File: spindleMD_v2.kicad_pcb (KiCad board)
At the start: 2 copper layers, 72 x 95 mm, 99 parts, among them J1 Conn_LogicPower, J2 Conn_SWD, J3 Conn_UART, J4 Conn_I2C, J5 Conn_Encoder, J6 Conn_GPIO, J7 Conn_MotorPower, J8 Conn_drivePower, J9 Conn_Motor, Q1 Q_NMOS_GDS, Q2 Q_NMOS_GDS, Q3 Q_NMOS_GDS, Q4 Q_NMOS_GDS, SW1 USER_BUTTON, SW2 RESET_BUTTON, U1 L7805, U10 ADuM3190, U2 L78L33_SOT89, U3 IK0505SA, U4 STM32F303K8Tx, U5 TLP152, U6 TLP152, U7 TLP152, U8 TLP152, U9 ACS712xLCTR-30A

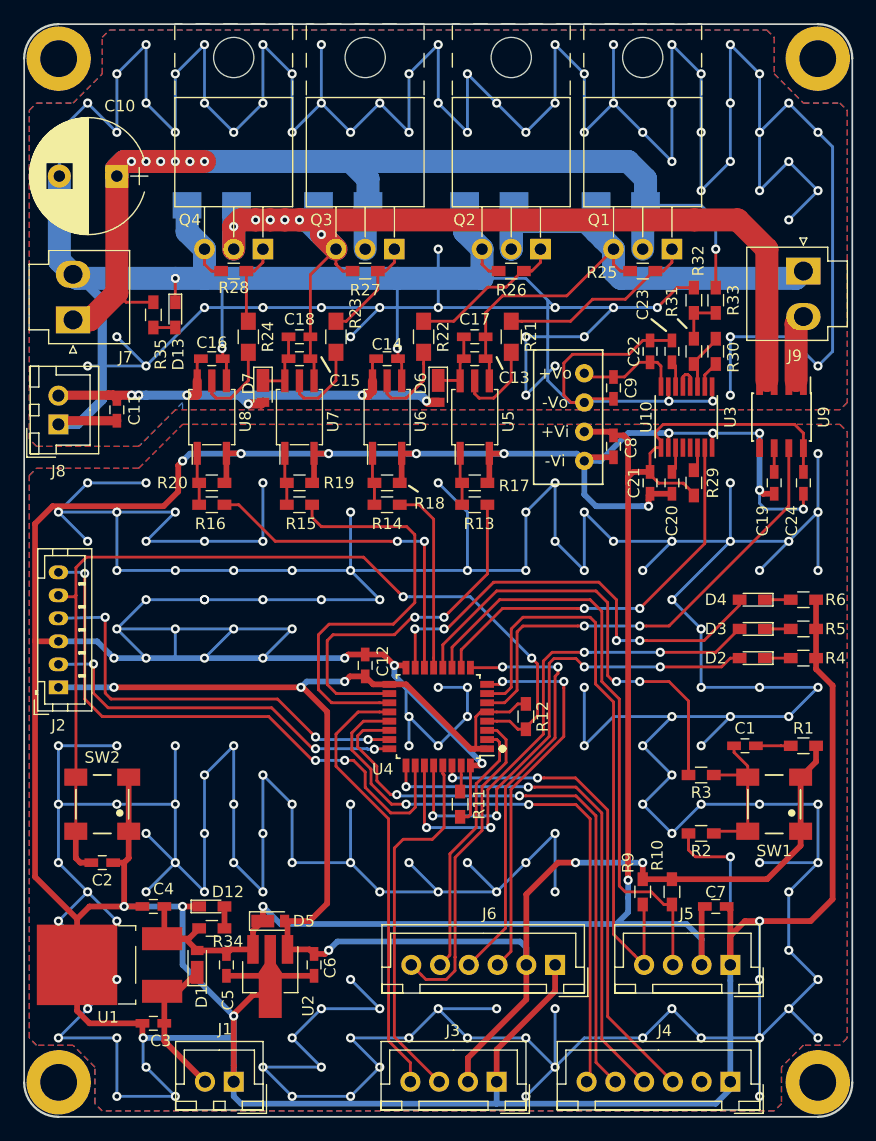
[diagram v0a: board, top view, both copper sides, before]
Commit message: シルク追加
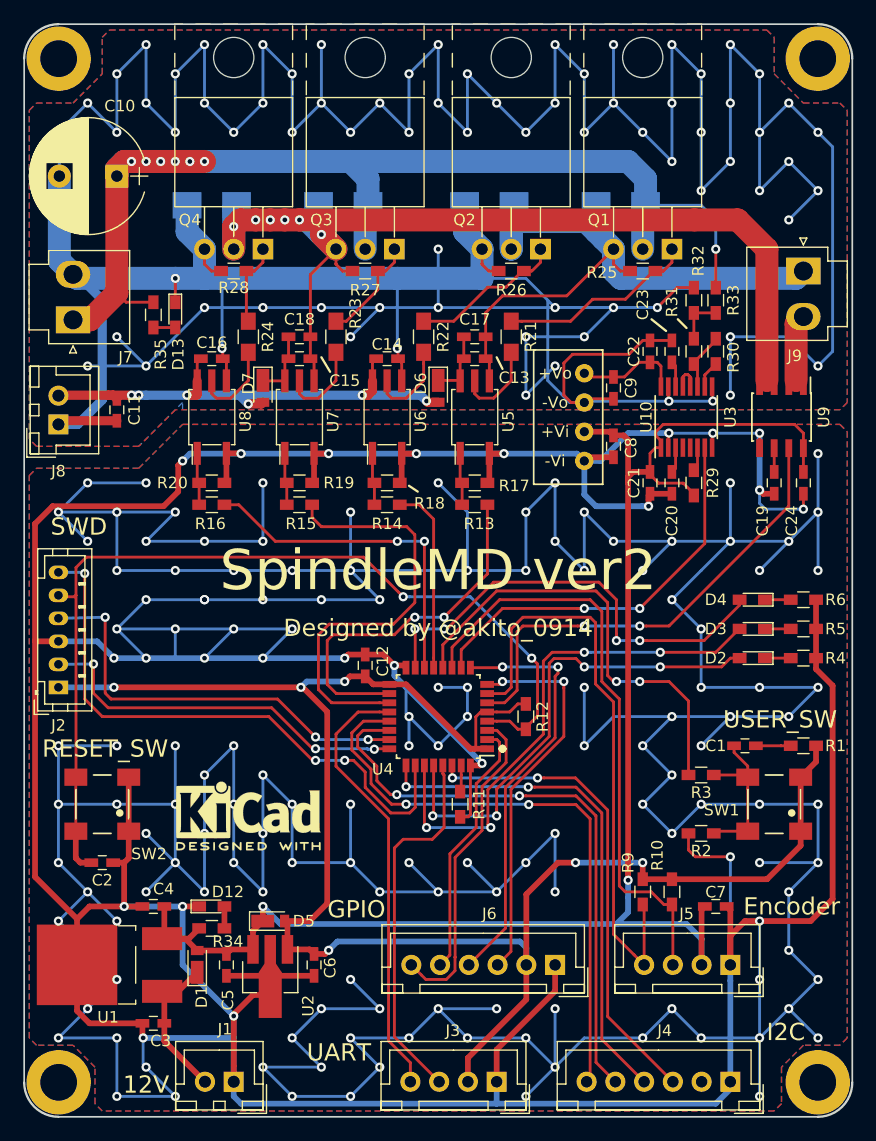
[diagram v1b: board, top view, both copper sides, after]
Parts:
- added G***: LOGO, my_footPrint:logo_EmergencyExit, B.Cu at (100.3, 110.4)
- added REF***: KiCad-Logo2_6mm_SilkScreen, Symbols:KiCad-Logo2_6mm_SilkScreen, F.Cu at (83.5, 121.3)
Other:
- board text added: "12V"
- board text added: "Designed by @akito_0914"
- board text added: "Encoder"
- board text added: "GPIO"
- board text added: "I2C"
- board text added: "RESET_SW"
- board text added: "SWD"
- board text added: "SpindleMD ver2"
- board text added: "UART"
- board text added: "USER_SW"
